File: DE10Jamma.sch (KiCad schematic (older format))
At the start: 104 parts, among them J1 Arduino 3-7, J10 5V TO DE10, J2 Arduino 8-SCL, J3 FAN 12V, J4 FAN 5V, J5 FAN 3V3, J6 Arduino Reset, J7 GPIO1, J8 Jamma_con, J9 CPS1 KICK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

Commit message: clean before sending to manufacture
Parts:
- added J11: 0.1\" kick, Connector_PinHeader_2.54mm:PinHeader_1x10_P2.54mm_Vertical, symbol Connector:Conn_01x10_Male
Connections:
- net GND: now also J11.1 (Pin_1), J11.2 (Pin_2)
- net JAMMA_P1_BUTTON4: now also J11.3 (Pin_3)
- net JAMMA_P1_BUTTON5: now also J11.4 (Pin_4)
- net JAMMA_P1_BUTTON6: now also J11.5 (Pin_5)
- net JAMMA_P2_BUTTON4: now also J11.7 (Pin_7)
- net JAMMA_P2_BUTTON5: now also J11.8 (Pin_8)
- net JAMMA_P2_BUTTON6: now also J11.9 (Pin_9)
- no-connect marks 21 -> 23
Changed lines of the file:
@@
 	1    0    0    -1
 $EndComp
+$Comp
+L Connector:Conn_01x10_Male J11
+U 1 1 5F09C1E4
+P 13050 3050
+F 0 "J11" H 13150 3650 50  0000 R CNN
+F 1 "0.1\" kick" H 13350 3550 50  0000 R CNN
+F 2 "Connector_PinHeader_2.54mm:PinHeader_1x10_P2.54mm_Vertical" H 13050 3050 50  0001 C CNN
+F 3 "~" H 13050 3050 50  0001 C CNN
+	1    13050 3050
+	1    0    0    1
+$EndComp
+Wire Wire Line
+	13250 2650 13850 2650
+Connection ~ 13850 2650
+Wire Wire Line
+	13850 2750 13250 2750
+Connection ~ 13850 2750
+Wire Wire Line
+	13850 2850 13250 2850
+Connection ~ 13850 2850
+Wire Wire Line
+	13850 3050 13250 3050
+Connection ~ 13850 3050
+Wire Wire Line
+	13850 3150 13250 3150
+Connection ~ 13850 3150
+Wire Wire Line
+	13850 3250 13250 3250
+Connection ~ 13850 3250
+Wire Wire Line
+	13850 3350 13250 3350
+Connection ~ 13850 3350
+Wire Wire Line
+	13850 3450 13250 3450
+Connection ~ 13850 3450
+NoConn ~ 13250 2950
+NoConn ~ 13250 2550
 $EndSCHEMATC

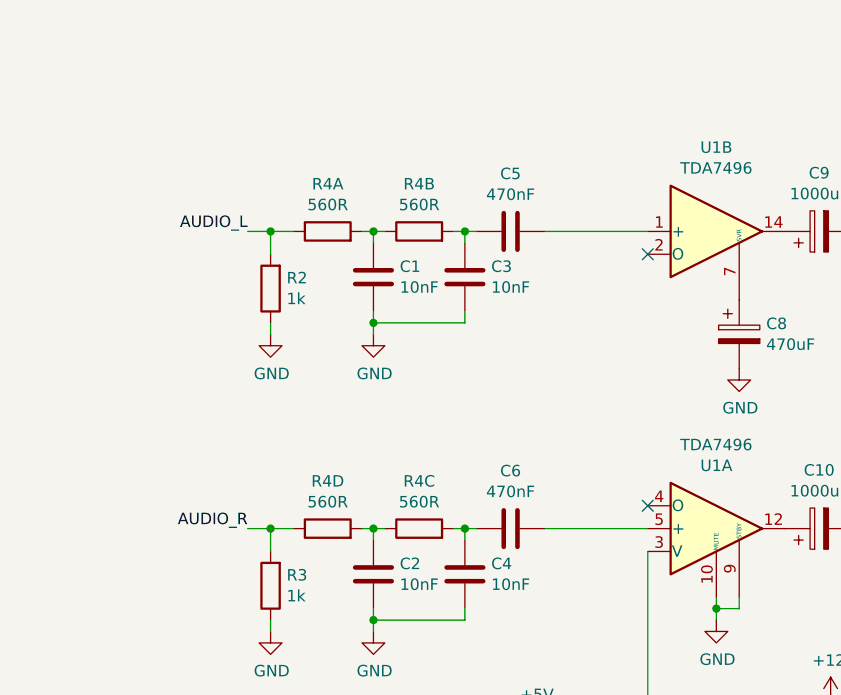
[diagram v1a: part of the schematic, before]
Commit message: Add mono/stereo jumper. Remove out of date pdf
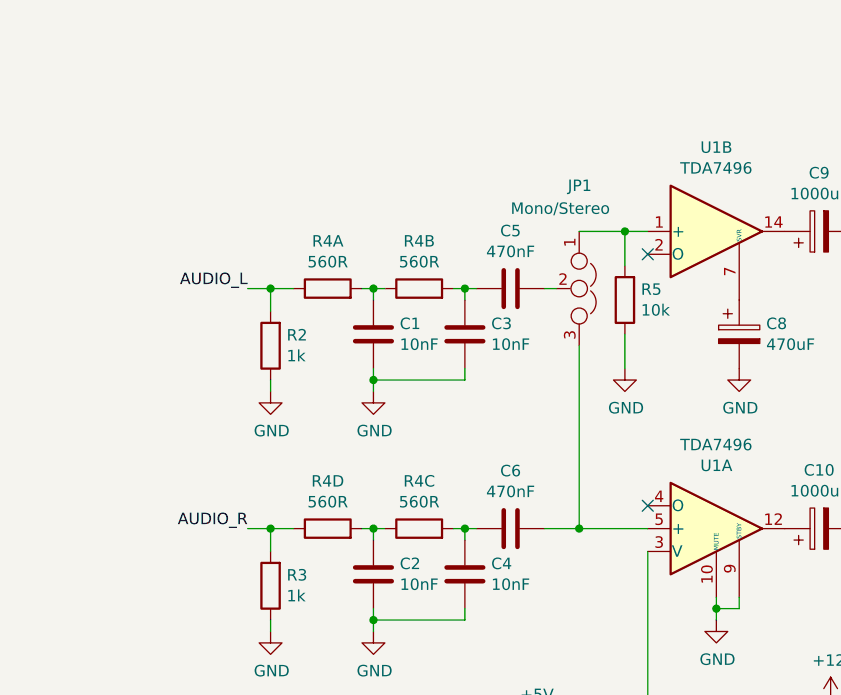
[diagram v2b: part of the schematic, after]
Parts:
- added JP1: Mono/Stereo, Connector_PinHeader_2.54mm:PinHeader_1x03_P2.54mm_Vertical, symbol Device:Jumper_NC_Dual
- added R5: 10k, Capacitor_SMD:C_0805_2012Metric, symbol Device:R
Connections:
- net GND: now also R5.1
- net at C6.2, U1.5 (+): now also JP1.3
- net at U1.1 (+): now also JP1.1, R5.2; no longer C5.2
- new net: C5.2, JP1.2
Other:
- moved on the sheet: C1, C3, C5, R2, R4A, R4B
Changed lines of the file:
@@
 L Device:R_Pack04_Split R4
 U 1 1 606C7461
-P 3250 4300
-F 0 "R4" V 3457 4300 50  0000 C CNN
-F 1 "560R" V 3366 4300 50  0000 C CNN
-F 2 "Resistor_SMD:R_Array_Convex_4x1206" V 3180 4300 50  0001 C CNN
-F 3 "~" H 3250 4300 50  0001 C CNN
-	1    3250 4300
+P 3250 4550
+F 0 "R4" V 3457 4550 50  0000 C CNN
+F 1 "560R" V 3366 4550 50  0000 C CNN
+F 2 "Resistor_SMD:R_Array_Convex_4x1206" V 3180 4550 50  0001 C CNN
+F 3 "~" H 3250 4550 50  0001 C CNN
+	1    3250 4550
 	0    -1   -1   0
 $EndComp
@@
 L Device:C C1
 U 1 1 606DE548
-P 3450 4500
-F 0 "C1" H 3565 4546 50  0000 L CNN
-F 1 "10nF" H 3565 4455 50  0000 L CNN
-F 2 "Capacitor_SMD:C_0805_2012Metric" H 3488 4350 50  0001 C CNN
-F 3 "~" H 3450 4500 50  0001 C CNN
-	1    3450 4500
+P 3450 4750
+F 0 "C1" H 3565 4796 50  0000 L CNN
+F 1 "10nF" H 3565 4705 50  0000 L CNN
+F 2 "Capacitor_SMD:C_0805_2012Metric" H 3488 4600 50  0001 C CNN
+F 3 "~" H 3450 4750 50  0001 C CNN
+	1    3450 4750
 	1    0    0    -1
 $EndComp
@@
 L Device:R_Pack04_Split R4
 U 2 1 606F5A5C
-P 3650 4300
-F 0 "R4" V 3857 4300 50  0000 C CNN
-F 1 "560R" V 3766 4300 50  0000 C CNN
-F 2 "Resistor_SMD:R_Array_Convex_4x1206" V 3580 4300 50  0001 C CNN
-F 3 "~" H 3650 4300 50  0001 C CNN
-	2    3650 4300
+P 3650 4550
+F 0 "R4" V 3857 4550 50  0000 C CNN
+F 1 "560R" V 3766 4550 50  0000 C CNN
+F 2 "Resistor_SMD:R_Array_Convex_4x1206" V 3580 4550 50  0001 C CNN
+F 3 "~" H 3650 4550 50  0001 C CNN
+	2    3650 4550
 	0    -1   -1   0
 $EndComp
@@
 L Device:C C3
 U 1 1 606F5A62
-P 3850 4500
-F 0 "C3" H 3965 4546 50  0000 L CNN
-F 1 "10nF" H 3965 4455 50  0000 L CNN
-F 2 "Capacitor_SMD:C_0805_2012Metric" H 3888 4350 50  0001 C CNN
-F 3 "~" H 3850 4500 50  0001 C CNN
-	1    3850 4500
+P 3850 4750
+F 0 "C3" H 3965 4796 50  0000 L CNN
+F 1 "10nF" H 3965 4705 50  0000 L CNN
+F 2 "Capacitor_SMD:C_0805_2012Metric" H 3888 4600 50  0001 C CNN
+F 3 "~" H 3850 4750 50  0001 C CNN
+	1    3850 4750
 	1    0    0    -1
 $EndComp
@@
 L power:GND #PWR013
 U 1 1 6071028D
-P 3450 4750
-F 0 "#PWR013" H 3450 4500 50  0001 C CNN
-F 1 "GND" H 3455 4577 50  0000 C CNN
-F 2 "" H 3450 4750 50  0001 C CNN
-F 3 "" H 3450 4750 50  0001 C CNN
-	1    3450 4750
-	1    0    0    -1
-$EndComp
-Text Label 2900 4300 2    50   ~ 0
+P 3450 5000
+F 0 "#PWR013" H 3450 4750 50  0001 C CNN
+F 1 "GND" H 3455 4827 50  0000 C CNN
+F 2 "" H 3450 5000 50  0001 C CNN
+F 3 "" H 3450 5000 50  0001 C CNN
+	1    3450 5000
+	1    0    0    -1
+$EndComp
+Text Label 2900 4550 2    50   ~ 0
 AUDIO_L
 Wire Wire Line
-	3400 4300 3450 4300
-Wire Wire Line
-	3450 4350 3450 4300
-Connection ~ 3450 4300
-Wire Wire Line
-	3450 4300 3500 4300
-Wire Wire Line
-	3450 4750 3450 4700
-Wire Wire Line
-	3850 4650 3850 4700
-Wire Wire Line
-	3850 4700 3450 4700
-Connection ~ 3450 4700
-Wire Wire Line
-	3450 4700 3450 4650
-Wire Wire Line
-	3800 4300 3850 4300
-Wire Wire Line
-	3850 4350 3850 4300
-Connection ~ 3850 4300
-Wire Wire Line
-	3850 4300 3900 4300
+	3400 4550 3450 4550
+Wire Wire Line
+	3450 4600 3450 4550
+Connection ~ 3450 4550
+Wire Wire Line
+	3450 4550 3500 4550
+Wire Wire Line
+	3450 5000 3450 4950
+Wire Wire Line
+	3850 4900 3850 4950
+Wire Wire Line
+	3850 4950 3450 4950
+Connection ~ 3450 4950
+Wire Wire Line
+	3450 4950 3450 4900
+Wire Wire Line
+	3800 4550 3850 4550
+Wire Wire Line
+	3850 4600 3850 4550
+Connection ~ 3850 4550
+Wire Wire Line
+	3850 4550 3900 4550
 $Comp
 L Device:R_Pack04_Split R4
@@
 	1    0    0    -1
 $EndComp
-Wire Wire Line
-	4200 4300 4650 4300
 $Comp
 L Device:CP C8
@@
 JAMMA_SPEAKER_L
 Wire Wire Line
-	4200 5600 4650 5600
+	4200 5600 4350 5600
 $Comp
 L Device:CP C10
@@
 Connection ~ 3000 5600
 Wire Wire Line
-	2900 4300 3000 4300
+	2900 4550 3000 4550
 Wire Wire Line
 	3000 6050 3000 6000
@@
 L Device:C C5
 U 1 1 63B18539
-P 4050 4300
-F 0 "C5" V 4302 4300 50  0000 C CNN
-F 1 "470nF" V 4211 4300 50  0000 C CNN
-F 2 "Capacitor_SMD:C_0805_2012Metric" H 4088 4150 50  0001 C CNN
-F 3 "~" H 4050 4300 50  0001 C CNN
-	1    4050 4300
+P 4050 4550
+F 0 "C5" V 4302 4550 50  0000 C CNN
+F 1 "470nF" V 4211 4550 50  0000 C CNN
+F 2 "Capacitor_SMD:C_0805_2012Metric" H 4088 4400 50  0001 C CNN
+F 3 "~" H 4050 4550 50  0001 C CNN
+	1    4050 4550
 	0    -1   -1   0
 $EndComp
@@
 L Device:R R2
 U 1 1 5EA08E01
-P 3000 4550
-F 0 "R2" H 2930 4504 50  0000 R CNN
-F 1 "1k" H 2930 4595 50  0000 R CNN
-F 2 "Capacitor_SMD:C_0805_2012Metric" V 2930 4550 50  0001 C CNN
-F 3 "~" H 3000 4550 50  0001 C CNN
-	1    3000 4550
+P 3000 4800
+F 0 "R2" H 2930 4754 50  0000 R CNN
+F 1 "1k" H 2930 4845 50  0000 R CNN
+F 2 "Capacitor_SMD:C_0805_2012Metric" V 2930 4800 50  0001 C CNN
+F 3 "~" H 3000 4800 50  0001 C CNN
+	1    3000 4800
 	-1   0    0    1
 $EndComp
@@
 L power:GND #PWR09
 U 1 1 5EA08E07
-P 3000 4750
-F 0 "#PWR09" H 3000 4500 50  0001 C CNN
-F 1 "GND" H 3005 4577 50  0000 C CNN
-F 2 "" H 3000 4750 50  0001 C CNN
-F 3 "" H 3000 4750 50  0001 C CNN
-	1    3000 4750
-	1    0    0    -1
-$EndComp
-Wire Wire Line
-	3000 4400 3000 4300
-Wire Wire Line
-	3000 4750 3000 4700
-Connection ~ 3000 4300
-Wire Wire Line
-	3000 4300 3100 4300
+P 3000 5000
+F 0 "#PWR09" H 3000 4750 50  0001 C CNN
+F 1 "GND" H 3005 4827 50  0000 C CNN
+F 2 "" H 3000 5000 50  0001 C CNN
+F 3 "" H 3000 5000 50  0001 C CNN
+	1    3000 5000
+	1    0    0    -1
+$EndComp
+Wire Wire Line
+	3000 4650 3000 4550
+Wire Wire Line
+	3000 5000 3000 4950
+Connection ~ 3000 4550
+Wire Wire Line
+	3000 4550 3100 4550
 Text Notes 15200 8400 2    50   ~ 0
 5V output to DE10, which has overvolt protection circuit.
@@
 NoConn ~ 13250 2950
 NoConn ~ 13250 2550
+$Comp
+L Device:R R5
+U 1 1 5F06479A
+P 4550 4600
+F 0 "R5" H 4480 4554 50  0000 R CNN
+F 1 "10k" H 4480 4645 50  0000 R CNN
+F 2 "Capacitor_SMD:C_0805_2012Metric" V 4480 4600 50  0001 C CNN
+F 3 "~" H 4550 4600 50  0001 C CNN
+	1    4550 4600
+	-1   0    0    1
+$EndComp
+$Comp
+L Device:Jumper_NC_Dual JP1
+U 1 1 5F0E7294
+P 4350 4550
+F 0 "JP1" V 3900 4500 50  0000 L CNN
+F 1 "Mono/Stereo" V 4000 4250 50  0000 L CNN
+F 2 "Connector_PinHeader_2.54mm:PinHeader_1x03_P2.54mm_Vertical" H 4350 4550 50  0001 C CNN
+F 3 "~" H 4350 4550 50  0001 C CNN
+	1    4350 4550
+	0    1    1    0
+$EndComp
+Wire Wire Line
+	4200 4550 4250 4550
+Wire Wire Line
+	4650 4300 4550 4300
+Wire Wire Line
+	4550 4450 4550 4300
+Connection ~ 4550 4300
+Wire Wire Line
+	4550 4300 4350 4300
+$Comp
+L power:GND #PWR0101
+U 1 1 5F3BE937
+P 4550 4900
+F 0 "#PWR0101" H 4550 4650 50  0001 C CNN
+F 1 "GND" H 4555 4727 50  0000 C CNN
+F 2 "" H 4550 4900 50  0001 C CNN
+F 3 "" H 4550 4900 50  0001 C CNN
+	1    4550 4900
+	1    0    0    -1
+$EndComp
+Wire Wire Line
+	4550 4900 4550 4750
+Wire Wire Line
+	4350 4800 4350 5600
+Connection ~ 4350 5600
+Wire Wire Line
+	4350 5600 4650 5600
 $EndSCHEMATC

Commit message: Use smaller footprint for r-packs. Rework mono/stereo jumper to avoid potential DC path issues if inputs have DC offset. General routing & silk screen cleanup.
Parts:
- removed R5: 10k, Capacitor_SMD:C_0805_2012Metric, symbol Device:R
- H5, H6, H7, H8: symbol Mechanical:MountingHole -> Mechanical:MountingHole_Pad
- R100, R101, R102, R103, R104, R105, R106, R107, R108, R109, R110, R111, R112, R113, R114, R4: footprint Resistor_SMD:R_Array_Convex_4x1206 -> Resistor_SMD:R_Array_Convex_4x0603
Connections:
- net GND: now also H5.1, H6.1, H7.1, H8.1, R104.6, R109.3, R114.6; no longer R104.7, R109.2, R114.7
- net at JP1.1: now also C5.1; no longer U1.1 (+)
- net at JP1.2: now also C3.1, R4.2; no longer C5.2
- net at C6.2, U1.5 (+): no longer JP1.3
- net at R106.1, R107.4, R108.5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: now also R109.2; no longer R109.3
- net at R106.2, R109.1: now also R109.6, R109.7; no longer R109.6, R109.7
- net at R101.8, R102.5, R103.4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: now also R104.7; no longer R104.6
- net at R111.8, R112.5, R113.4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: now also R114.7; no longer R114.6
- net at R111.7, R114.8: now also R114.2, R114.3; no longer R114.2, R114.3
- net at R101.7, R104.8: now also R104.2, R104.3; no longer R104.2, R104.3
- net at C4.1, C6.1, R4.3: now also JP1.3
- new net: C5.2, U1.1 (+)
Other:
- moved on the sheet: C5, C6, JP1
